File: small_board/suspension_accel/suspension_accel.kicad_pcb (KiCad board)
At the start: 4 copper layers, 20 x 74 mm, 38 parts, among them IC1 TJA1050T_CM,118, IC2 AMS1117-3.3, IC3 SN74LVC1T45DCKR, IC4 ESP32-S3-MINI-1-N8, IC5 ADS1220IPWR, IC6 TLV75533PDBVR, IC7 SN74LVC1T45DCKR, J1 OSTTE040104, J2 BM04B-GVHS-TB_LF__SN_

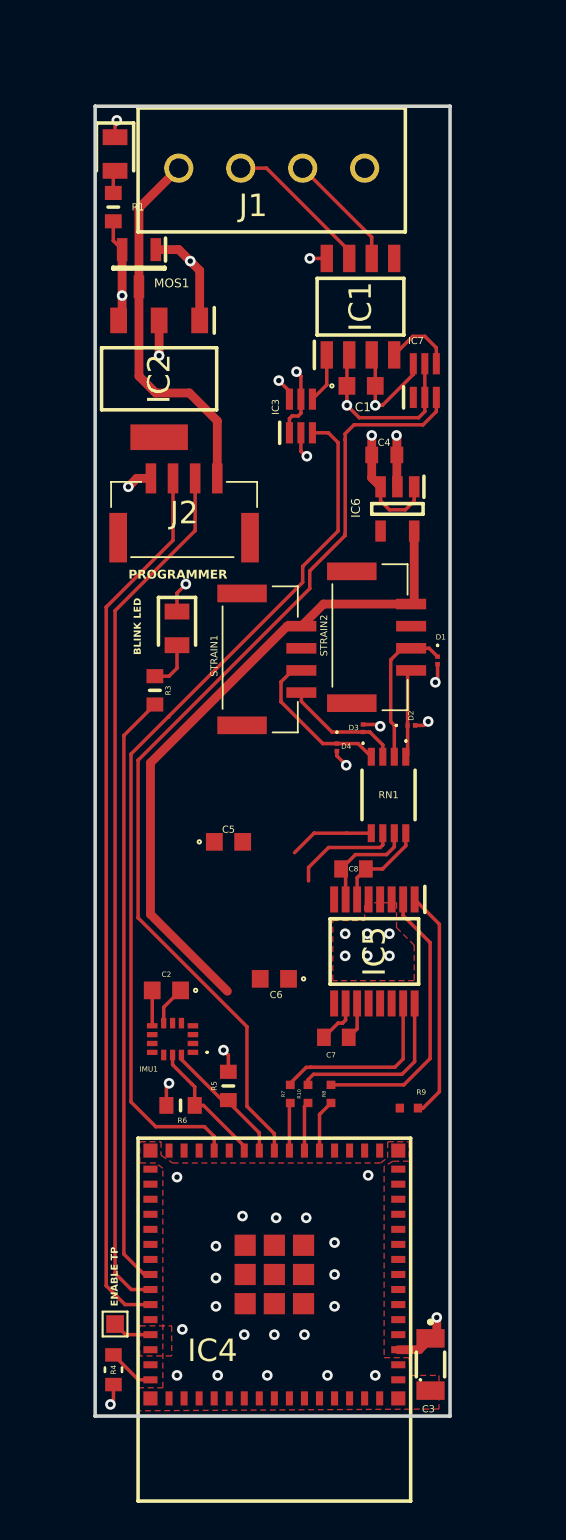
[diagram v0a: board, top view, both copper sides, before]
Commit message: finished routing, added logo, widened board for DRC compliance
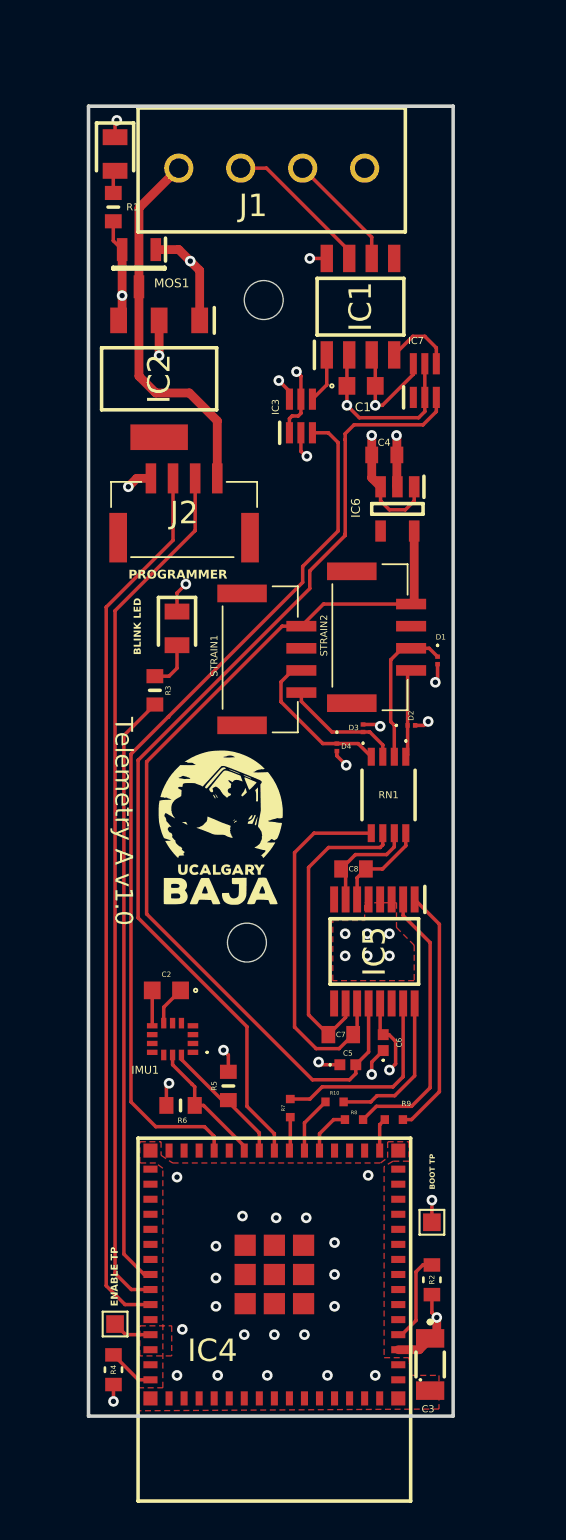
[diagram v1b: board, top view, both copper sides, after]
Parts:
- added G***: LOGO, Library:baja_logo, F.Cu at (29.4, 64.7)
- added R2: RR0816P-103-D, Library:RESC1608X60N, F.Cu at (41.4, 90.3)
- added REF**: MountingHole_2.2mm_M2, MountingHole:MountingHole_2.2mm_M2, F.Cu at (31.9, 35.0)
- added REF**: MountingHole_2.2mm_M2, MountingHole:MountingHole_2.2mm_M2, F.Cu at (30.9, 71.2)
- added REF**: TestPoint_Pad_1.0x1.0mm, TestPoint:TestPoint_Pad_1.0x1.0mm, F.Cu at (41.4, 87.0)
- C5, C6: value C0603C104K5RACTU -> C0402C104K9RACTU; footprint Library:C0603 -> Library:C0402C104J4RACTU
- moved C5 14.3 mm to (36.6, 78.2)
- moved C6 7.13 mm to (38.6, 76.9), turned to 90 degrees
- moved R8 1.95 mm to (37.0, 81.2), turned to 0 degrees
- moved R10 1.57 mm to (35.9, 80.2), turned to 0 degrees
- moved R9 1.07 mm to (39.2, 81.2)
- moved R7 0.80 mm to (33.4, 80.6)
- moved C7 0.29 mm to (36.2, 76.5)
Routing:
- net Net-(IC5-AIN0/REFP1): track 6.90 -> 20.6 mm
- net Net-(IC4-IO18): track 40.1 -> 53.4 mm
- net Net-(IC5-AIN1): track 8.71 -> 17.5 mm
- net +3.3V: track 15.3 -> 20.9 mm, vias 6 -> 7
- net Net-(IC4-IO0): track 0.37 -> 5.32 mm
- net GND: track 34.6 -> 38.7 mm, vias 38 -> 41
- net Net-(IC4-IO12): track 0.00 -> 1.87 mm
- net Net-(IC5-DIN): track 10.0 -> 8.71 mm
- net Net-(IC5-SCLK): track 13.0 -> 14.2 mm
- net Net-(IC5-DOUT/~{DRDY}): track 10.2 -> 11.0 mm
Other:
- board size 20 x 74 mm -> 20.6 x 74 mm
- board text added: "BOOT TP"
- board text added: "Telemetry A v1.0"

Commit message: Added copper layers for each net, adding cool slikscreen stuff
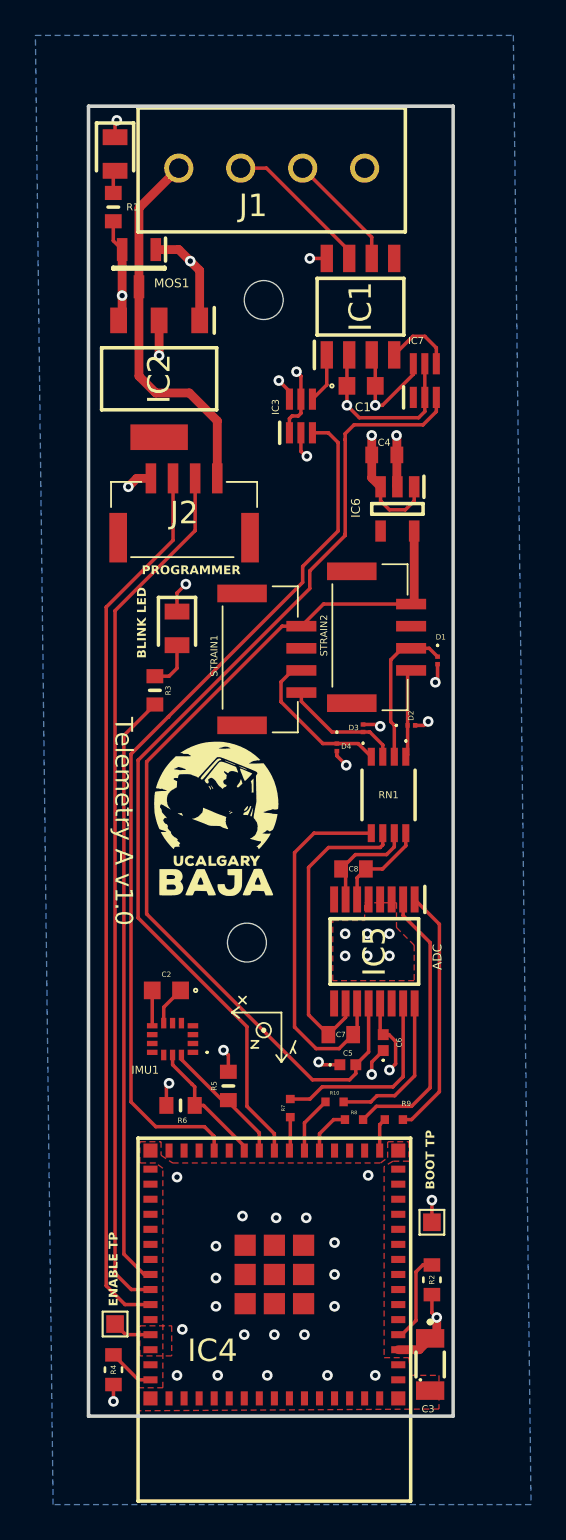
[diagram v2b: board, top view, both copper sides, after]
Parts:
- added G***: LOGO, Library:canada, B.Cu at (35.1, 77.4)
- added G***: LOGO, Library:tire_tracks, B.Cu at (24.5, 90.2)
- added REF**: IMU_vectors, Library:IMU_vectors, F.Cu at (32.9, 75.2)
- added REF**: Symbol_ESD-Logo-Text_CopperTop, Symbol:Symbol_ESD-Logo-Text_CopperTop, B.Cu at (32.1, 46.8)
- moved G*** 0.56 mm to (29.2, 64.2)
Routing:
- added copper zone on In2.Cu, net +3.3V
- added copper zone on B.Cu, net +5V
- added copper zone on In1.Cu, net GND
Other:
- board text added: "ADC"
- board text added: "Designed Early 2026"

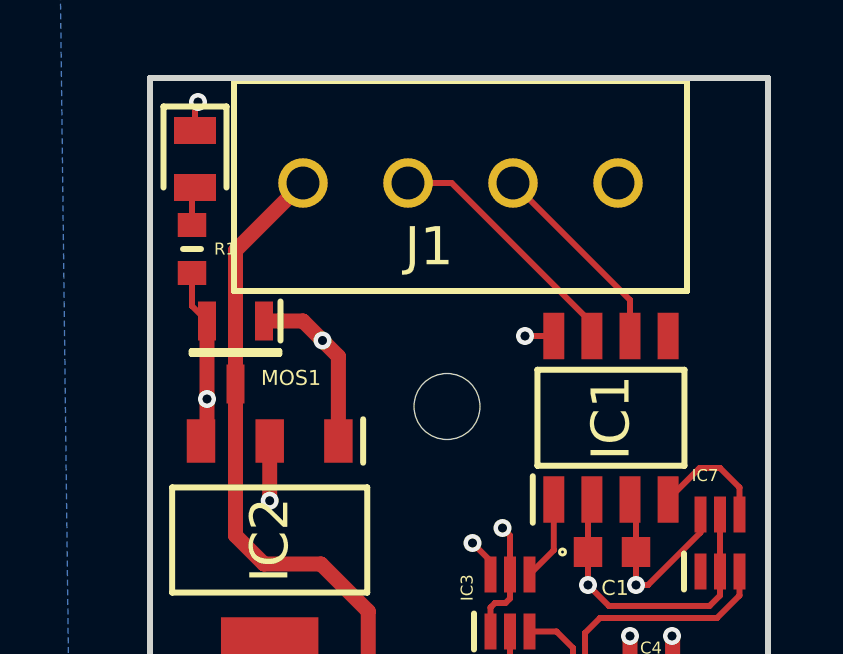
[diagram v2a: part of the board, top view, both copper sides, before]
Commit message: added supply line TVS
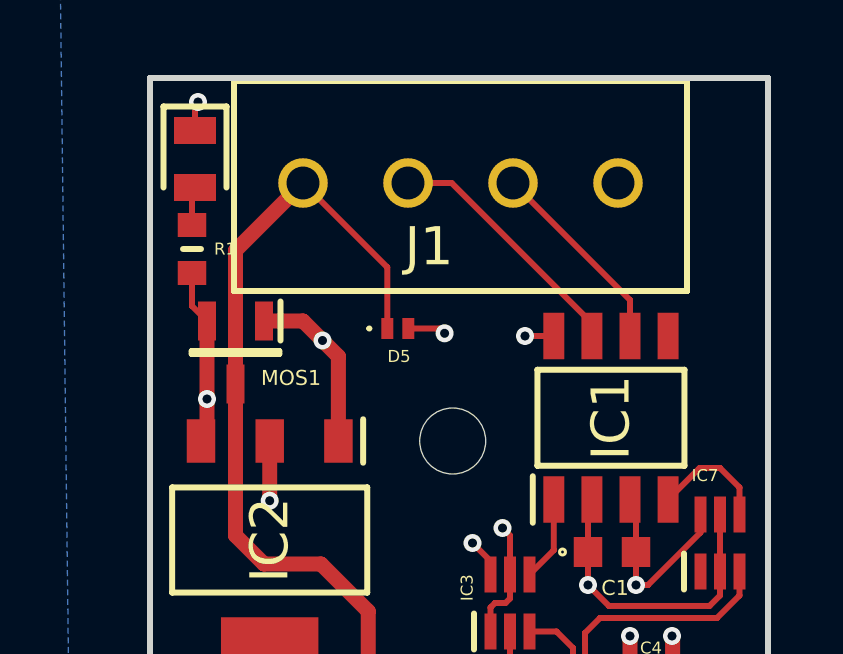
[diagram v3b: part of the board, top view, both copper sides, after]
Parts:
- added D5: D5V0F1U2LP-7B, Library:D5V0F1U2LP7B, F.Cu at (30.3, 32.4)
- moved REF** 1.17 mm to (32.1, 36.1)
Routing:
- net Net-(D5-K): track 21.4 -> 27.4 mm
- net GND: track 38.7 -> 40.0 mm, vias 41 -> 42

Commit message: prepared for manufacturing first iter
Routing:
- net GND: track 40.0 -> 44.8 mm, vias 42 -> 44
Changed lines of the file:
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@@
 			)
 		)
+		(model "/home/marcus/Desktop/telemetry_pcb_1/small_board/components/LIB_D5V0F1U2LP-7B/D5V0F1U2LP-7B/3D/D5V0F1U2LP-7B.stp"
+			(offset
+				(xyz 0 0 0)
+			)
+			(scale
+				(xyz 1 1 1)
+			)
+			(rotate
+				(xyz -90 -0 -0)
+			)
+		)
 	)
 	(footprint "MountingHole:MountingHole_2.2mm_M2"
@@
 			)
 		)
+		(model "/home/marcus/Desktop/telemetry_pcb_1/small_board/components/LIB_RCLAMP3521ZATFT/RCLAMP3521ZATFT/3D/RCLAMP3521ZATFT.stp"
+			(offset
+				(xyz 0 0 0)
+			)
+			(scale
+				(xyz 1 1 1)
+			)
+			(rotate
+				(xyz 0 0 0)
+			)
+		)
 	)
 	(footprint "Library:RESC1608X60N"
@@
 			)
 		)
+		(model "/home/marcus/Desktop/telemetry_pcb_1/small_board/components/LIB_RCLAMP3521ZATFT/RCLAMP3521ZATFT/3D/RCLAMP3521ZATFT.stp"
+			(offset
+				(xyz 0 0 0)
+			)
+			(scale
+				(xyz 1 1 1)
+			)
+			(rotate
+				(xyz 0 0 0)
+			)
+		)
 	)
 	(footprint "Library:canada"
@@
 			(at -0.13716 -13.4493 0)
 			(layer "B.SilkS")
+			(hide yes)
 			(effects
 				(font
@@
 	)
 	(segment
+		(start 33.055 54.625)
+		(end 32.11 55.57)
+		(width 0.2)
+		(layer "F.Cu")
+		(net 2)
+	)
+	(segment
 		(start 34 42.45)
 		(end 34 43.5)
@@
 	)
 	(segment
+		(start 34.025 54.625)
+		(end 33.055 54.625)
+		(width 0.2)
+		(layer "F.Cu")
+		(net 2)
+	)
+	(segment
 		(start 38.378 58.928)
 		(end 38.48 59.03)
@@
 	)
 	(segment
+		(start 40.225 53.375)
+		(end 38.675 53.375)
+		(width 0.2)
+		(layer "F.Cu")
+		(net 2)
+	)
+	(segment
 		(start 38.65 77.35)
 		(end 38 78)
@@
 	)
 	(segment
+		(start 38.675 53.375)
+		(end 38 54.05)
+		(width 0.2)
+		(layer "F.Cu")
+		(net 2)
+	)
+	(segment
 		(start 27.75 32.75)
 		(end 28.28 33.28)
@@
 		(net 2)
 	)
+	(segment
+		(start 32.11 55.57)
+		(end 32.08 55.6)
+		(width 0.2)
+		(layer "F.Cu")
+		(net 2)
+	)
+	(via
+		(at 32.11 55.57)
+		(size 0.6)
+		(drill 0.3)
+		(layers "F.Cu" "B.Cu")
+		(net 2)
+	)
 	(via
 		(at 35 78)
@@
 	)
 	(via
+		(at 38.03 54.03)
+		(size 0.6)
+		(drill 0.3)
+		(layers "F.Cu" "B.Cu")
+		(net 2)
+	)
+	(via
 		(at 39 72)
 		(size 0.6)
@@
 		(hatch edge 0.5)
 		(priority 3)
-		(connect_pads
+		(connect_pads yes
 			(clearance 0)
 		)

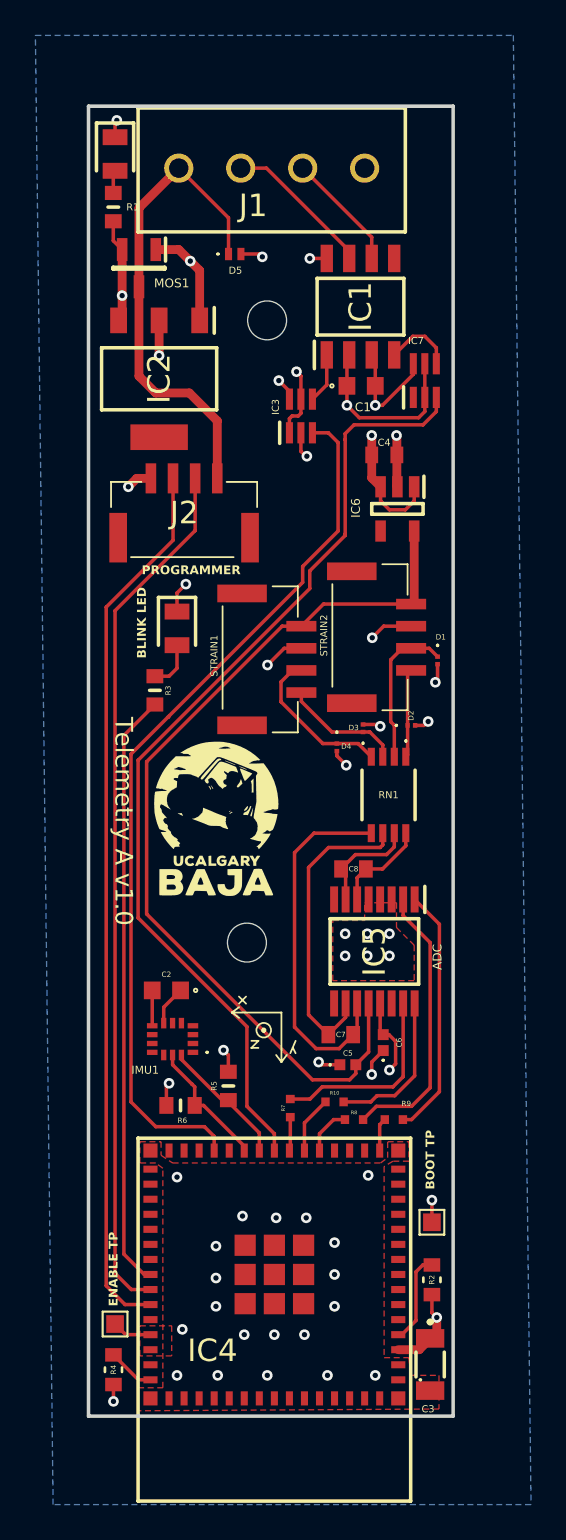
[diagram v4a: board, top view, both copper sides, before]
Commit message: spaced out routing a bit
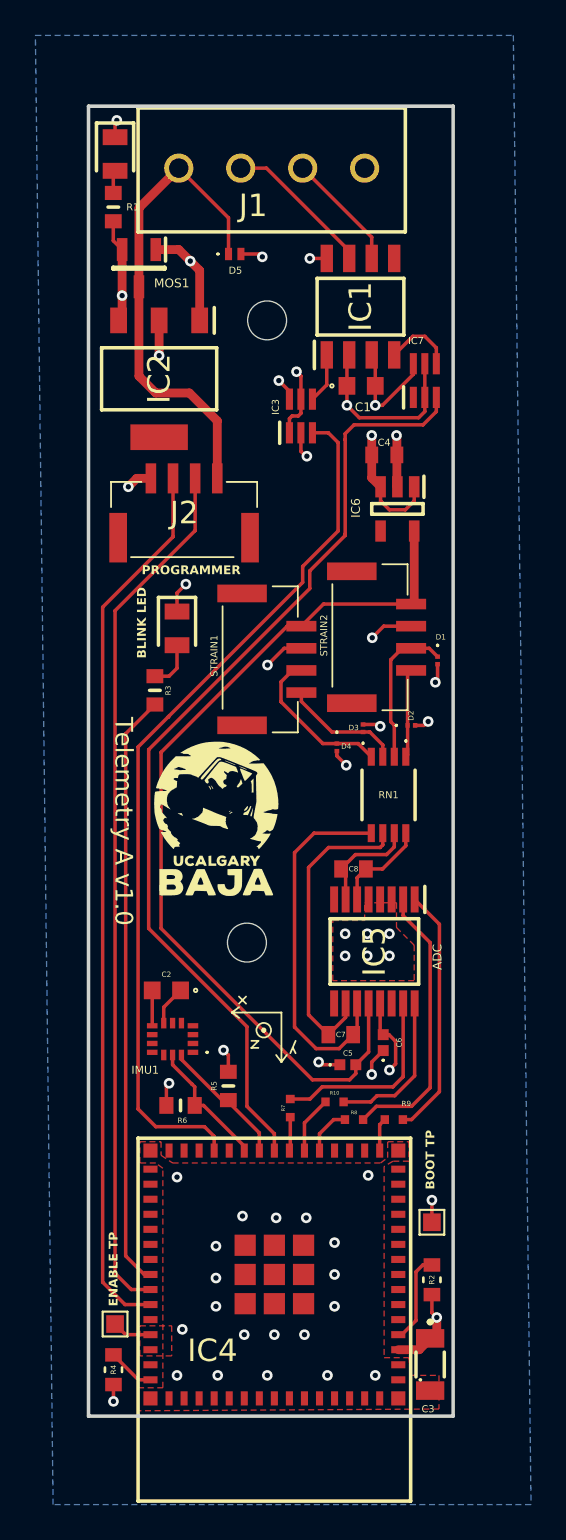
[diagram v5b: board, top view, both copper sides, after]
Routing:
- net Net-(IC4-IO18): track 53.4 -> 52.6 mm
